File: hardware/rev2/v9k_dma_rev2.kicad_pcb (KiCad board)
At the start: 2 copper layers, 81.3 x 8 mm, 38 parts, among them IC1 SN74LVC1G04, J10 EXPANDER GPIO, J3 microSD, J4 OLED SPI, J5 ENCODER, J6 ACT LED, J7 ESP32 BREAKOUT, J8 DEBUG UART, J9 SWD, U1 WeAct RP2350B Core, U3 ESP32-S3-WROOM-1U-N16R8, U4 LD1117V33, U5 MCP23S17

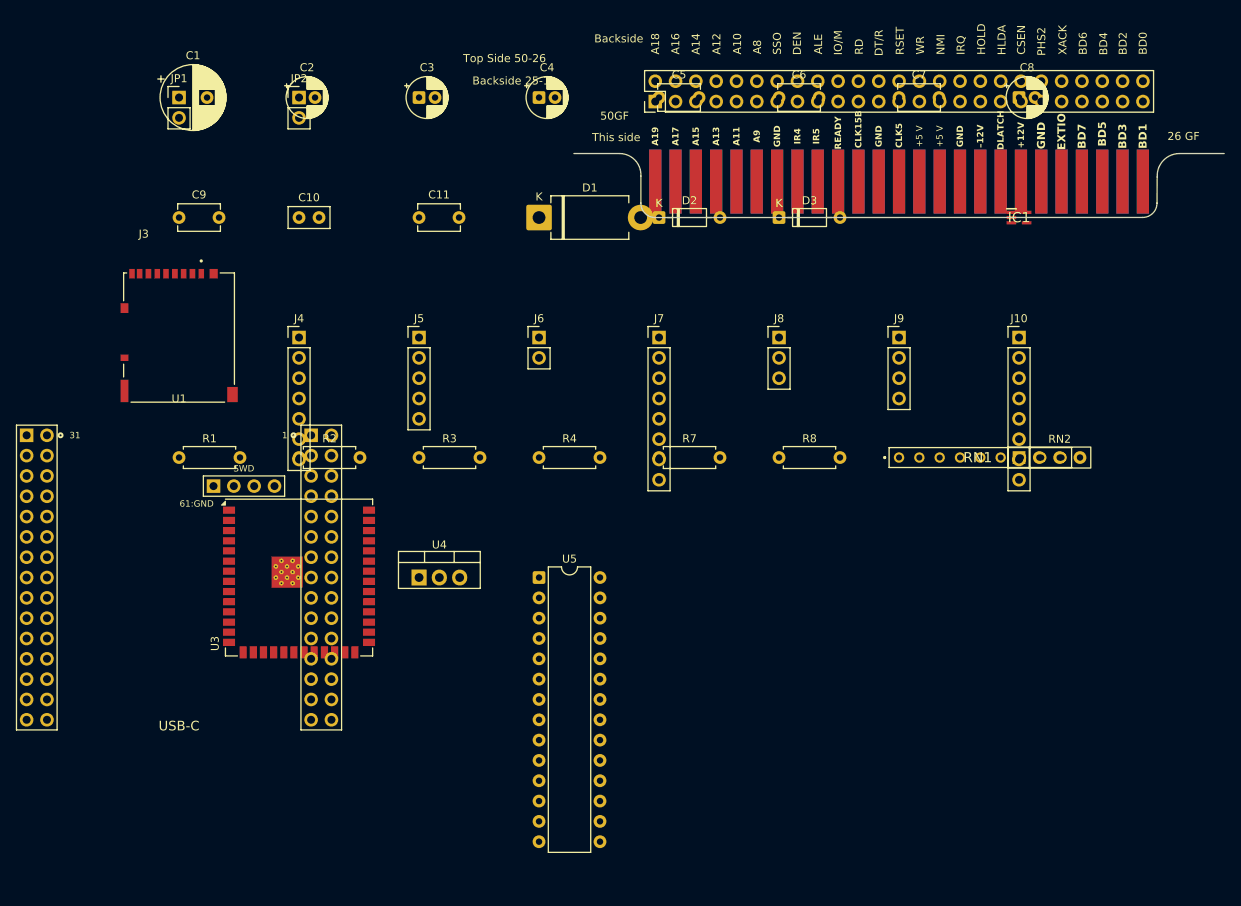
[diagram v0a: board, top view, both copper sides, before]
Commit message: v9k_dma_rev2: complete stages 4-6 — placed, routed (ROUTE OK), BOM finalized
- Placement + routing via llm_autoroute (margin-1 sweep winner): 122/122 nets,
  4940mm track, 252 vias, GND pours ~60% both layers, 0 unrouted, 0 hard DRC
  (kicad-cli verified; 68 cosmetic silk items remain). R3/R4/C8 moved clear of
  the USB-C plug path per review.
- U3 WROOM thermal vias enlarged to 0.3mm drill (board min-hole conflict);
  J3 edge-mount microSD edge-clearance exemption via v9k_dma_rev2.kicad_dru.
- Schematic: MPN fields populated from project.toml [[parts]] (19 symbols);
  U1/GF1 excluded from BOM (own stock / PCB feature).
- Stage 6: check-bom 0 errors, order_bom.csv $107.23 for 5 boards
  (DK $102.57 + Mouser $4.66); shunts for JP1/JP2 + 5x WeAct module are
  manual offsets.
- project.toml stage = 6 (all gates passed); skill_feedback.md items 14-25.
- .gitignore: llm_autoroute transient artifacts (pre-* backups, sweep logs).

Co-Authored-By: Claude Fable 5 <noreply@anthropic.com>
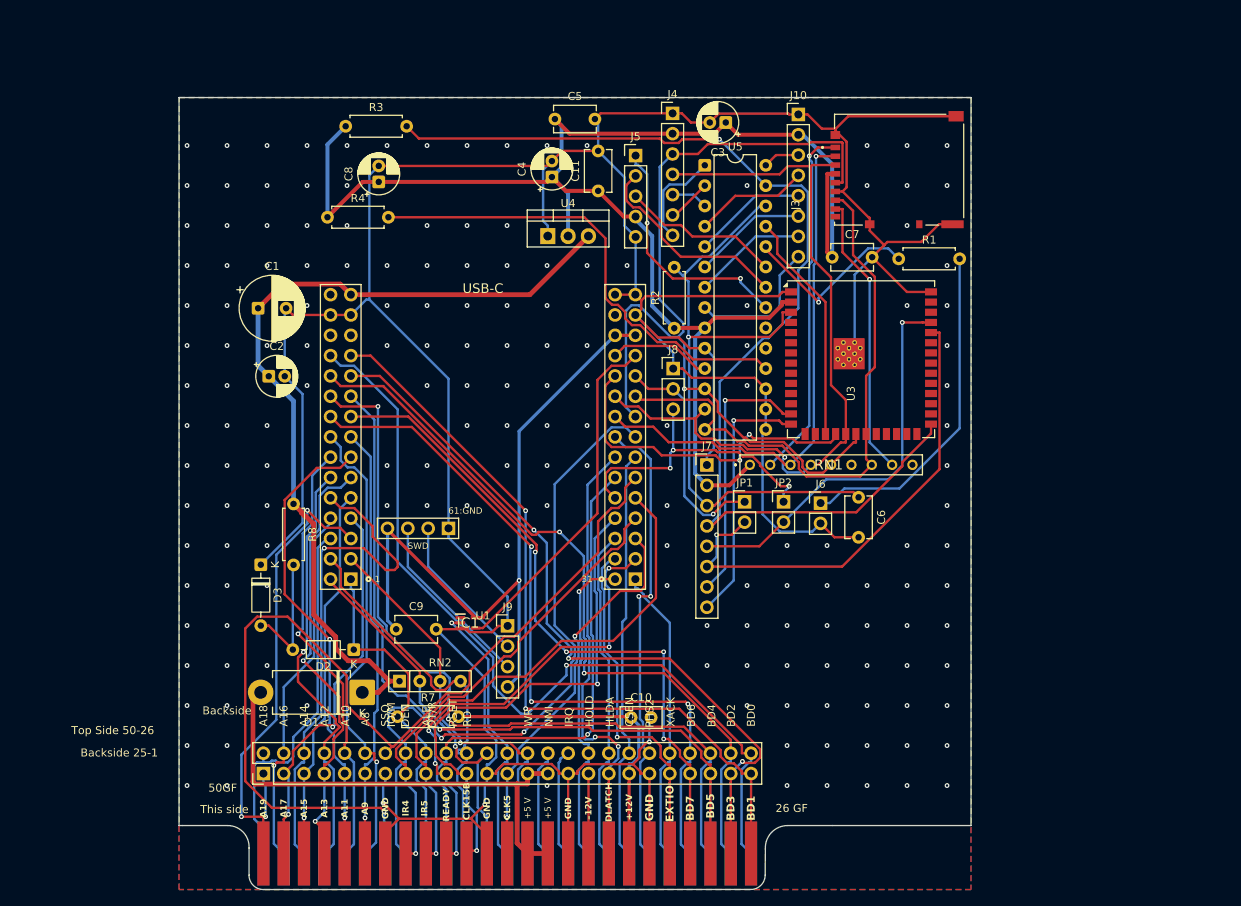
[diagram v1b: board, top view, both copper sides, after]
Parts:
- moved GF1 97.2 mm to (91.0, 149.0)
- moved R1 93.3 mm to (140.0, 70.2)
- moved J3 92.4 mm to (140.0, 59.0), turned to 90 degrees
- moved JP1 86.9 mm to (120.7, 100.5)
- moved IC1 85.5 mm to (86.1, 115.7)
- moved RN2 82.3 mm to (77.6, 123.0)
- moved C8 80.7 mm to (75.0, 60.5), turned to 90 degrees
- moved JP2 78.9 mm to (125.6, 100.5)
- moved D3 78.0 mm to (60.2, 108.4), turned to -90 degrees
- moved U3 75.4 mm to (135.2, 82.7)
- moved C10 75.0 mm to (106.5, 127.5)
- moved D2 66.1 mm to (71.8, 119.0), turned to 180 degrees
- moved D1 63.3 mm to (72.9, 124.4), turned to 180 degrees
- moved R8 61.0 mm to (64.3, 100.8), turned to -90 degrees
- moved J9 60.8 mm to (91.1, 116.0)
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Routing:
- net GND: track 0.00 -> 502.7 mm, vias 0 -> 173
- net +3V3_PERI: track 0.00 -> 192.1 mm
- net ESP_IO0: track 0.00 -> 135.7 mm, vias 0 -> 1
- net SSO: track 0.00 -> 121.0 mm, vias 0 -> 1
- net SPI1_SCK: track 0.00 -> 111.4 mm, vias 0 -> 1
- net BD0: track 0.00 -> 106.4 mm, vias 0 -> 1
- net +5V_RAIL: track 0.00 -> 106.4 mm
- net BD4: track 0.00 -> 99.0 mm, vias 0 -> 2
- net BD1: track 0.00 -> 96.8 mm, vias 0 -> 2
- net SPI1_MOSI: track 0.00 -> 95.3 mm, vias 0 -> 1
- net BD5: track 0.00 -> 94.4 mm, vias 0 -> 1
- net BD3: track 0.00 -> 93.4 mm, vias 0 -> 3
- net BD2: track 0.00 -> 93.2 mm, vias 0 -> 2
- net BD6: track 0.00 -> 91.0 mm, vias 0 -> 3
- net 3V3_WEACT: track 0.00 -> 88.3 mm, vias 0 -> 1
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- added copper zone on B.Cu, net GND
- added copper zone on F.Cu, net GND
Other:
- board size 81.3 x 8 mm -> 99 x 91 mm
